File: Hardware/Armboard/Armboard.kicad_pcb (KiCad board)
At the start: 2 copper layers, 125.5 x 100.8 mm, 117 parts, among them J1 Test_Point, SW1 SW_Push, SW2 SW_Push, SW3 SW_Push, SW4 SW_Push, SW5 SW_Push, SW6 SW_Push, U1 OKI, U2 TM4C129E_Launchpad

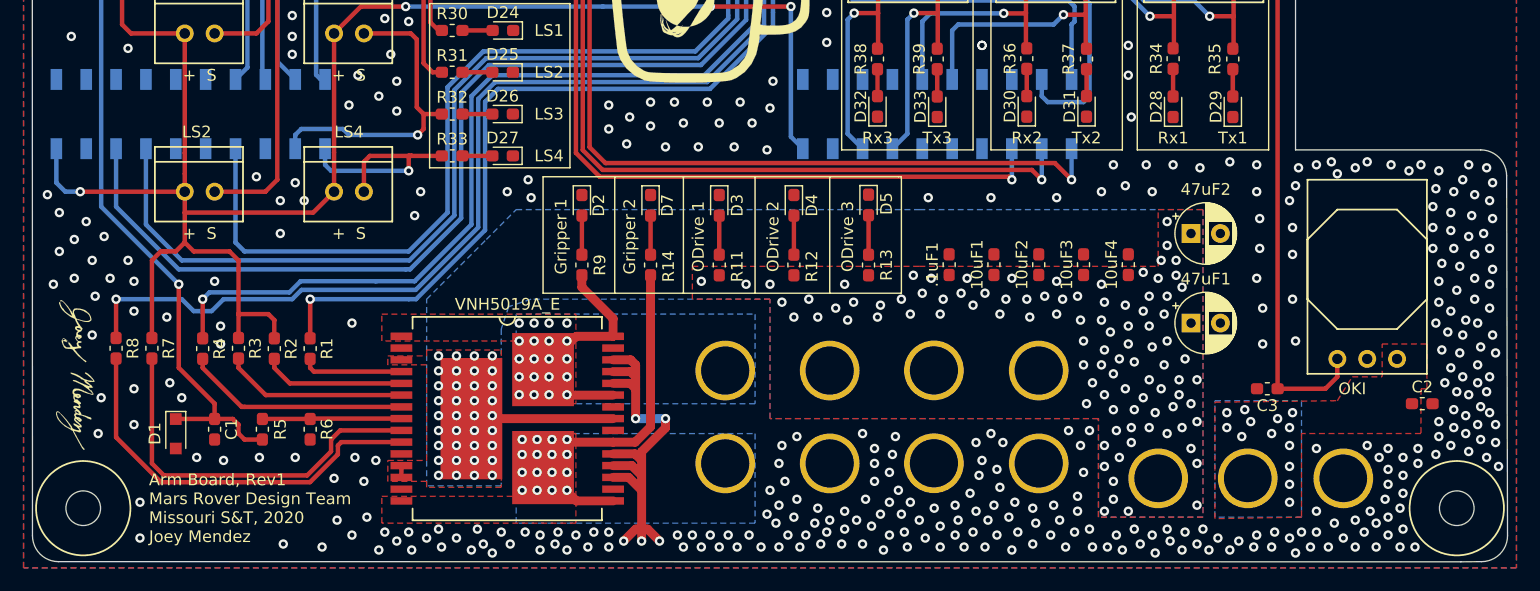
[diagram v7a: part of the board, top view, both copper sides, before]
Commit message: less vias
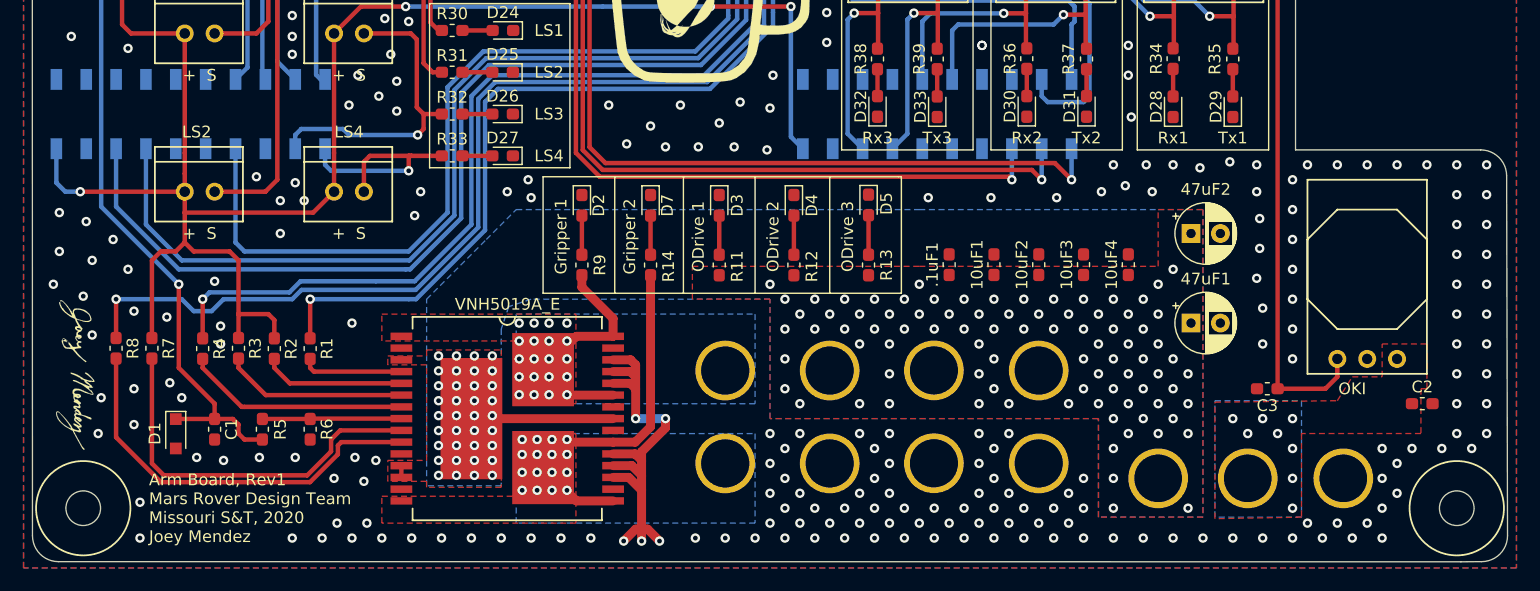
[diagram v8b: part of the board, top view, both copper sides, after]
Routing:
- net GND: vias 467 -> 318
- net +12V: vias 134 -> 123
- net +12L: vias 13 -> 8
